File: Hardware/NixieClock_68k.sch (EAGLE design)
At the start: 18 parts

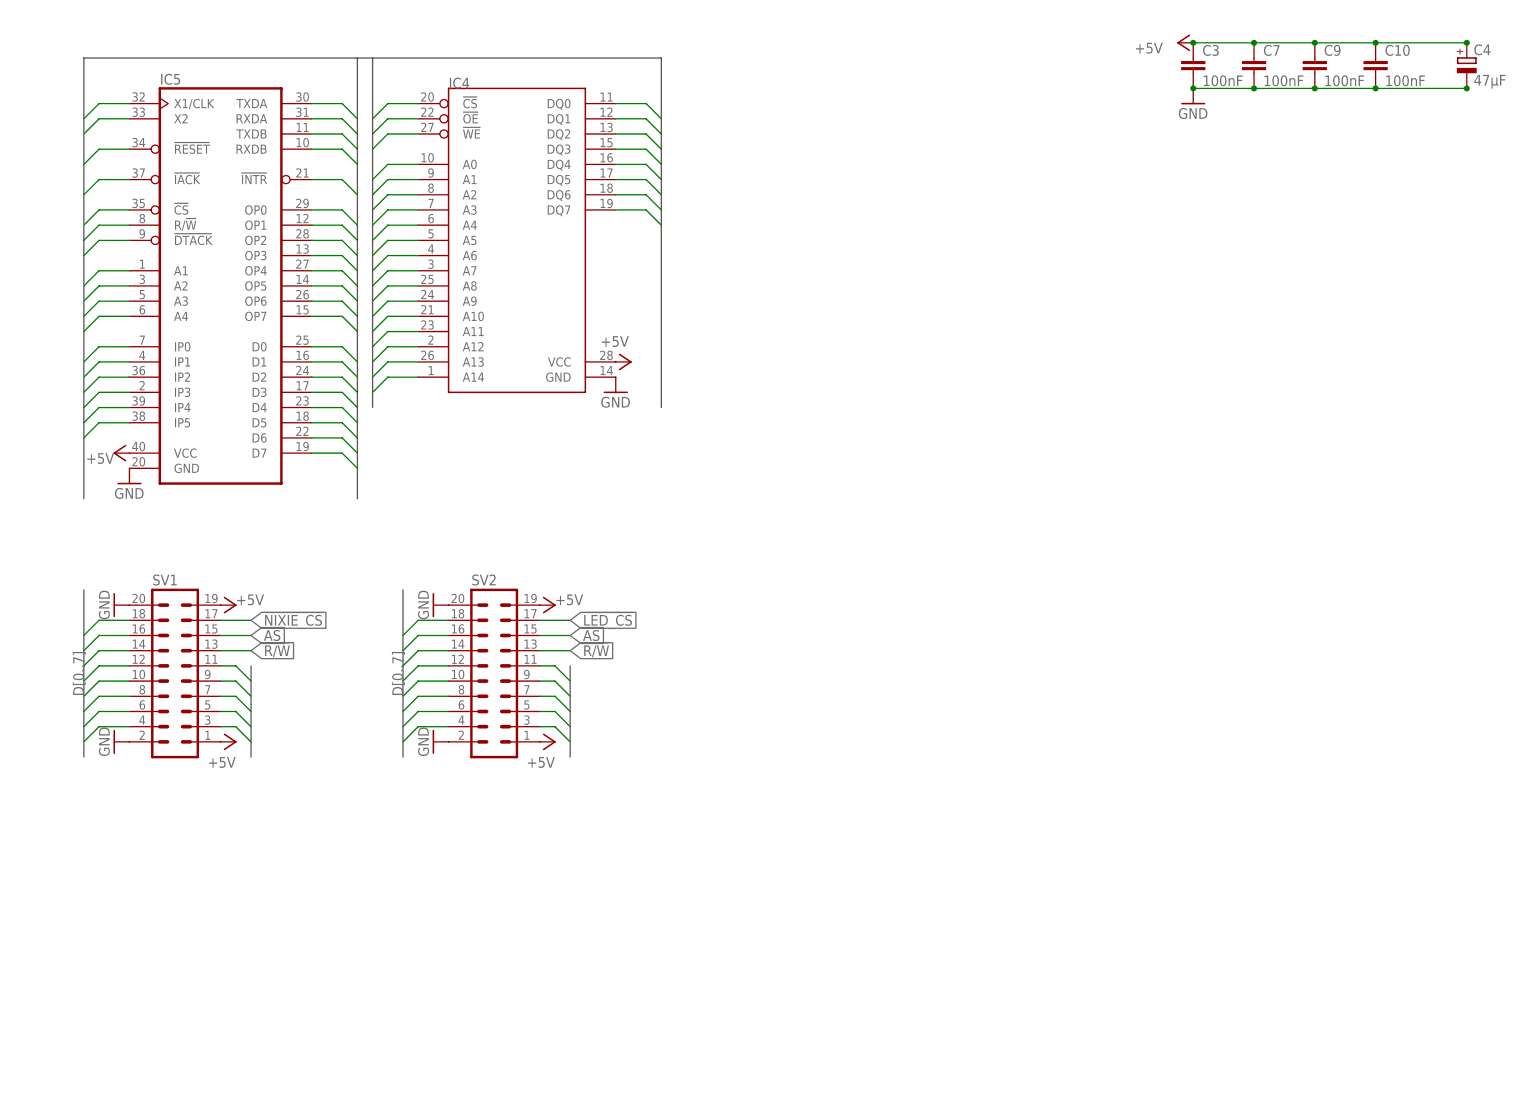
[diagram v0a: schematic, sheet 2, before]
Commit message: Replaced 68681 with FT245R; added header for VFD
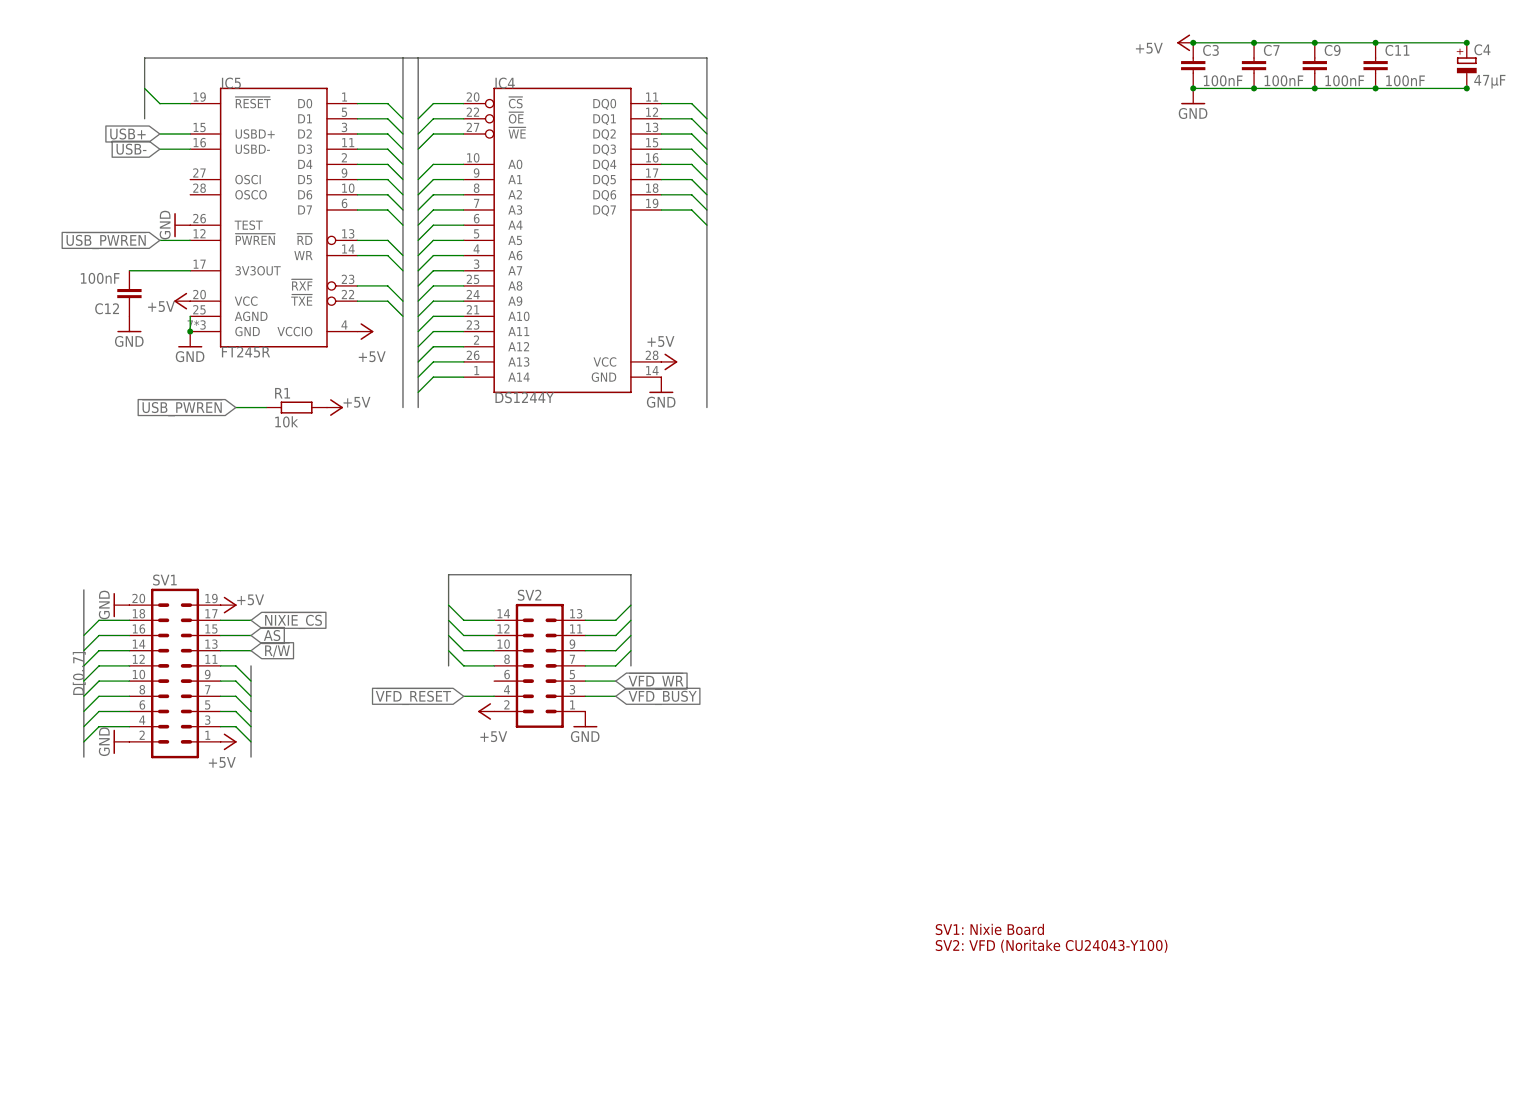
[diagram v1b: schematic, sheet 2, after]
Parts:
- added C11, C12: 100nF, rcl:C-EUC0805
- added R1: 10k, rcl:R-EU_R2012
- C10: value 100nF -> 47µF; device rcl:C-EUC0805 -> rcl:CPOL-EUCT6032; MOUSER 710-885012207072 -> 581-TAJD476M016RNJV
- IC1: value (none) -> 68008
- IC3: value (none) -> 39SF020
- IC4: value (none) -> DS1244Y
- IC5: value (none) -> FT245R; device Parts:MC68681DIP40 -> Parts:FT245RSSOP-28
- QG1: value (none) -> 4MHz; MOUSER (none) -> 774-MXO45HS-3C-4.0
- SV2: device con-lstb:MA10-2 -> con-lstb:MA07-2
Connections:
- removed net !68881_CS: IC5.!CS
- removed net !68881_DTACK: IC5.!DTACK
- removed net !68881_IACK: IC5.!IACK
- removed net !68881_IRQ: IC5.!INTR
- removed net !LED_CS: SV2.17
- removed net 68881_X1: IC5.X1/CLK
- removed net 68881_X2: IC5.X2
- removed net GPIO_IN0: IC5.IP0
- removed net GPIO_IN1: IC5.IP1
- removed net GPIO_IN2: IC5.IP2
- removed net GPIO_IN3: IC5.IP3
- removed net GPIO_IN4: IC5.IP4
- removed net GPIO_IN5: IC5.IP5
- removed net GPIO_OUT0: IC5.OP0
- removed net GPIO_OUT1: IC5.OP1
- removed net GPIO_OUT2: IC5.OP2
- removed net GPIO_OUT3: IC5.OP3
- removed net GPIO_OUT4: IC5.OP4
- removed net GPIO_OUT5: IC5.OP5
- removed net GPIO_OUT6: IC5.OP6
- removed net GPIO_OUT7: IC5.OP7
- removed net UART0_RX: IC5.RXDA
- removed net UART0_TX: IC5.TXDA
- removed net UART1_RX: IC5.RXDB
- removed net UART1_TX: IC5.TXDB
- new net !USB_PWREN: IC5.!PWREN, R1.1
- new net !USB_RD: IC5.!RD
- new net !USB_RXF: IC5.!RXF
- new net !USB_TXE: IC5.!TXE
- new net !VFD_RESET: SV2.4
- new net !VFD_WR: SV2.5
- new net N$1: C12.2, IC5.3V3OUT
- new net USB+: IC5.USBD+
- new net USB-: IC5.USBD-
- new net USB_WR: IC5.WR
- new net VFD_BUSY: SV2.3
- net !AS: no longer SV2.15
- net +5V: now also C10.+, C11.1, IC5.VCCIO, R1.2, SV2.2; no longer C10.1, SV2.1, SV2.19
- net A0: no longer IC5.A1, SV2.3
- net A1: no longer IC5.A2, SV2.5
- net A2: no longer IC5.A3, SV2.7
- net A3: no longer IC5.A4, SV2.9
- net A4: no longer SV2.11
- net D0: now also SV2.7; no longer SV2.4
- net D1: now also SV2.8; no longer SV2.6
- net D2: now also SV2.9; no longer SV2.8
- net D4: now also SV2.11; no longer SV2.12
- net D5: now also SV2.12; no longer SV2.14
- net D6: now also SV2.13; no longer SV2.16
- net D7: now also SV2.14; no longer SV2.18
- net GND: now also C10.-, C11.2, C12.1, IC5.AGND, IC5.TEST, SV2.1; no longer C10.2, SV2.2, SV2.20
- net R/!W!: no longer IC5.R/!W, SV2.13
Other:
- note added: "Memory Map: $00000 - $1FFFF: ROM $20000 - $3FFFF: RAM $40000 - $4FFFF: USB FIFO $50000 - $5FFFF: RTC $60000 - $6FFFF: Nixie output registers $70000 - $7FFFF: VFD"
- note added: "SV1: Nixie Board SV2: VFD (Noritake CU24043-Y100)"
- note removed: "Memory Map: $00000 - $1FFFF: ROM $20000 - $3FFFF: RAM $40000 - $4FFFF: 68881 $50000 - $5FFFF: RTC $60000 - $6FFFF: Nixie output registers $70000 - $7FFFF: LED displays"
- moved on the sheet: C1, C2, C5, C6, IC4

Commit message: basic address decoding
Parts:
- added C13, C15, C16, C17, C21: 100nF, rcl:C-EUC0805
- added C14, C20: 47µF, rcl:CPOL-EUCT6032
- added C18: 10nF, rcl:C-EUC0805
- added C19: 47nF, rcl:C-EUC0805
- added IC10, IC8: 74HC32N, 74xx-eu:74HC32N
- added IC6: NE555, st-microelectronics:NE555
- added IC7: 74HC137N, 74xx-eu:74HC137N
- added IC9: 74HC04N, 74xx-eu:74HC04N
- added R2: 4k7, rcl:R-EU_R2012
- added R3: 150k, rcl:R-EU_R2012
- added R4: 0R, rcl:R-EU_R2012
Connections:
- removed net !OE: IC2.!OE, IC3.!OE, IC4.!OE
- removed net !VFD_RESET: SV2.4
- new net !A15: IC8B.I1, IC9A.O
- new net !IO_CS: IC8B.O
- new net !NIXIE_IO_CS: IC7A.Y4, IC8A.I0, IC8B.I0
- new net !R!/W: IC8D.I1, IC9B.O
- new net !RAM_CS_0: IC7A.Y6
- new net !RAM_CS_1: IC7A.Y7
- new net !RAM_OE: IC2.!OE
- new net !ROM_CS_0: IC7A.Y0
- new net !ROM_CS_1: IC7A.Y1
- new net !ROM_OE: IC3.!OE
- new net !RTC_OE: IC4.!OE
- new net !USB_CS: IC7A.Y2, IC8C.I0, IC8D.I0
- new net !USB_WR: IC8C.O, IC9C.I
- new net !VFD_CS: IC10A.I0, IC7A.Y5
- new net 555_D: IC6.DIS, R2.1, R3.2
- new net 555_T: C19.1, IC6.TRE, IC6.TRI, R3.1
- new net N$2: C18.1, IC6.CON
- new net TIMER_IRQ: IC6.OUT
- net !AS: now also IC7A.G2, R4.2
- net !DTACK: now also R4.1
- net !NIXIE_CS: now also IC8A.O
- net !RESET: now also SV2.4
- net !RTC_CS: now also IC7A.Y3
- net !USB_RD: now also IC8D.O
- net !VFD_WR: now also IC10A.O
- net +5V: now also C13.1, C14.+, C15.1, C16.1, C17.1, C20.+, C21.1, IC10P.VCC, IC6./RES, IC6.VCC+, IC7A.G1, IC7P.VCC, IC8P.VCC, IC9P.VCC, R2.2
- net A15: now also IC8A.I1, IC9A.I
- net A16: now also IC7A.A
- net A17: now also IC7A.B
- net A18: now also IC7A.C
- net GND: now also C13.2, C14.-, C15.2, C16.2, C17.2, C18.2, C19.2, C20.-, C21.2, IC10P.GND, IC3.A17, IC3.A18, IC6.GND, IC7A.GL, IC7P.GND, IC8P.GND, IC9P.GND
- net R/!W!: now also IC10A.I1, IC8C.I1, IC9B.I
- net USB_WR: now also IC9C.O
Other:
- note added: "1x 100nF per 74xxx chip"
- note added: "IC6 triggers at ~100Hz, used as timer IRQ"
- note added: "Memory Map: $00000 - $1FFFF: ROM $20000 - $2FFFF: USB FIFO $30000 - $3FFFF: RTC $40000 - $47FFF: Nixie output registers $48000 - $4FFFF: IO registers $50000 - $5FFFF: VFD $60000 - $7FFFF: RAM Mirrored at $80000-$FFFFF"
- note added: "Zero waitstates for all memory OK up to 4MHz clock"
- note removed: "Memory Map: $00000 - $1FFFF: ROM $20000 - $3FFFF: RAM $40000 - $4FFFF: USB FIFO $50000 - $5FFFF: RTC $60000 - $6FFFF: Nixie output registers $70000 - $7FFFF: VFD"
